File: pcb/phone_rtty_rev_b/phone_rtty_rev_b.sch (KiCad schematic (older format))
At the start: 33 parts, among them J1 Phone, J2 Transceiver, P1 TRX Data, Q1 2N2222, Q2 2N2222, SW1 1200/9600

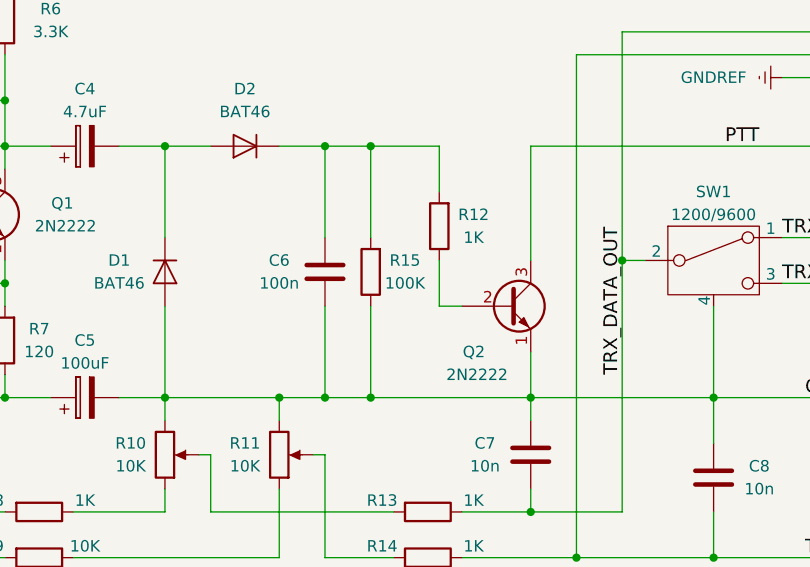
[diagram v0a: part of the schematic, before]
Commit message: Updated resistor value on the schematic.
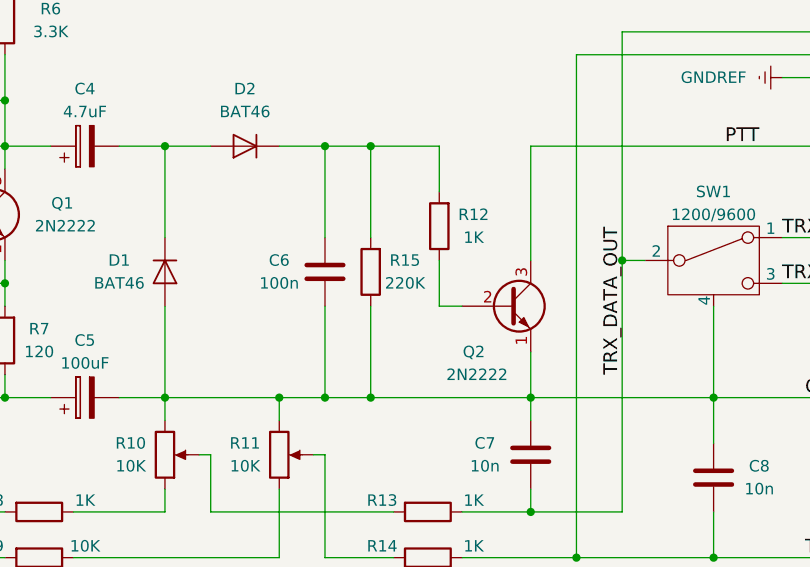
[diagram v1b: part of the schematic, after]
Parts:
- R15: value 100K -> 220K
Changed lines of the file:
@@
 P 6400 2850
 F 0 "R15" H 6250 2800 50  0000 C CNN
-F 1 "100K" H 6250 2900 50  0000 C CNN
+F 1 "220K" H 6250 2900 50  0000 C CNN
 F 2 "Resistors_THT:R_Axial_DIN0207_L6.3mm_D2.5mm_P10.16mm_Horizontal" V 6330 2850 50  0001 C CNN
 F 3 "" H 6400 2850 50  0000 C CNN
